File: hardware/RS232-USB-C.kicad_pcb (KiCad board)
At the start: 2 copper layers, 85.6 x 30.5 mm, 68 parts, among them J1 USB_C_Receptacle_USB2.0_16P, J10 NC, J11 UART, J12 NC, J13 NC, J2 DE9_Receptacle, J3* NC, J4 RXTX, J5 RTSCTS, J6 DTRDSR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

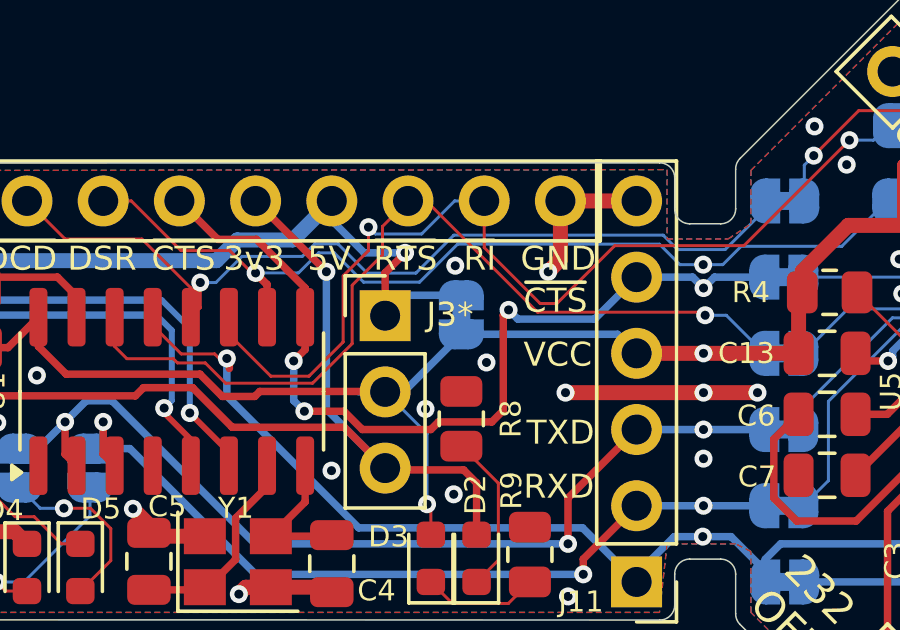
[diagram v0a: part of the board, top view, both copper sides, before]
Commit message: Tidy schematic
- Replaced criss-crossed wires with labels between IC/connectors
- Removed jumper 'values' where wasn't really needed
- repositioned references/values where hard to read
- gave components room to 'breathe'
- changed to regular (compared to small) components in most places to avoid cramping
- moved components around to be close to their logical section
- updated some symbols to be more standard/correct
- replaced 'NC' components to regularly labelled ones marked as DNP
- fixed sch->pcb linking on J3
- organized schematic into logical blocks
- uncommited the lockfile
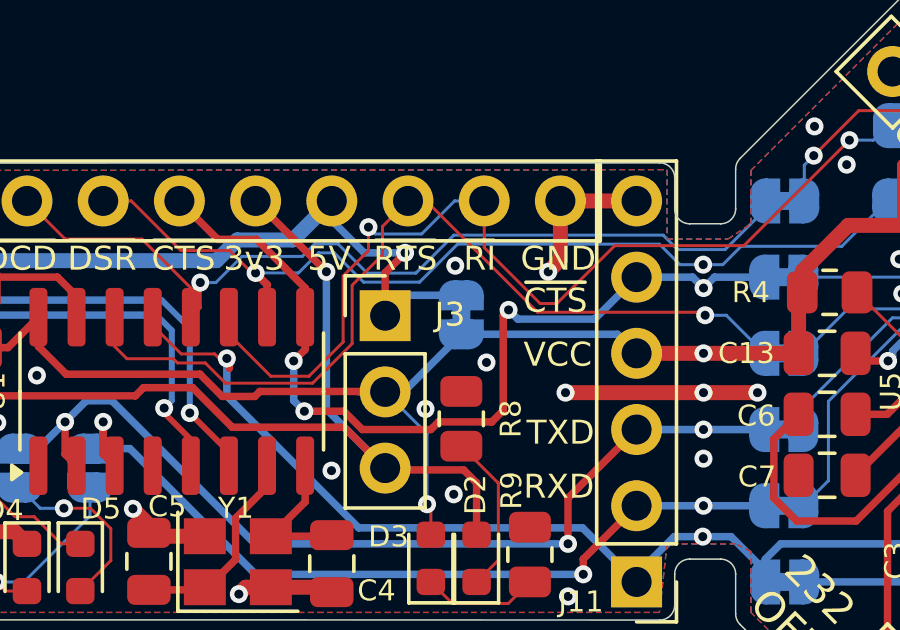
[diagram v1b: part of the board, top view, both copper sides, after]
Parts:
- J1: value USB_C_Receptacle_USB2.0_16P -> HOST
- J10: value NC -> SHUTDOWN
- J11: value UART -> FTDI_HEADER
- J12: value NC -> UART BUS
- J13: value NC -> EXT_PWR
- J3: renamed from J3*; value NC -> PWR_SEL
- J8: value NC -> RS232
- J9: value NC -> USB
- R3: value NC -> 5k1
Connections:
- net /VBUS renamed VBUS
- net /~{232STS} renamed Net-(U5-~{STATUS})
- net 232CTS renamed /232CTS
- net 232DCD renamed /232DCD
- net 232DSR renamed /232DSR
- net 232DTR renamed /232DTR
- net 232RI renamed /232RI
- net 232RTS renamed /232RTS
- net 232RxD renamed /232RxD
- net 232TxD renamed /232TxD
- net Net-(J1-CC1) renamed /CC1
- net Net-(J1-CC2) renamed /CC2
- net Net-(J1-SBU1) renamed /SBU1
- net Net-(J1-SBU2) renamed /SBU2
- net Net-(J1-SHIELD) renamed SHIELD
- net Net-(J4-Pin_2) renamed /DE9_P2
- net Net-(J4-Pin_3) renamed /DE9_P3
- net Net-(J5-Pin_2) renamed /DE9_P7
- net Net-(J5-Pin_3) renamed /DE9_P8
- net Net-(J6-Pin_2) renamed /DE9_P4
- net Net-(J6-Pin_3) renamed /DE9_P6
- net Net-(J7-Pin_2) renamed /DE9_P1
- net Net-(J9-Pin_5) renamed /D-B
- net Net-(J9-Pin_6) renamed /D+A
- net Net-(J9-Pin_7) renamed /D-A
- net Net-(J9-Pin_8) renamed /D+B
- net Net-(U1-XI) renamed /XI
- net Net-(U1-XO) renamed /XO
- J10 pad 1: GND -> /~{232SHD}
- J10 pad 2: /~{232SHD} -> GND
- J2 pad 0: (no net) -> GND
- J8 pad 10: (no net) -> unconnected-(J8-Pin_10-Pad10)
- J8 pad 5: GND -> /DE9_P5
- R5 pad 1: /3VEN -> Net-(U3-EN)
- U3 pad 3: /3VEN -> Net-(U3-EN)
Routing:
- net /DE9_P5: track 0.00 -> 12.0 mm
- net GND: track 110.7 -> 98.7 mm

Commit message: Rev 1
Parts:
- added C9: 100nF, Capacitor_SMD:C_0805_2012Metric, F.Cu at (137.4, 90.4)
- added JP24: 3v3 opt., Jumper:SolderJumper-2_P1.3mm_Open_RoundedPad1.0x1.5mm, B.Cu at (143.4, 88.9)
- moved J10 2.52 mm to (174.8, 96.0), turned to 45 degrees
- moved JP17 1.12 mm to (127.8, 92.7)
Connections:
- J8 pad 5: /DE9_P5 -> GND
- J9 pad 12: SHIELD -> +3V3
- R5 pad 1: Net-(U3-EN) -> /3VEN
- U1 pad 4: unconnected-(U1-V3-Pad4) -> Net-(JP24-A)
- U3 pad 3: Net-(U3-EN) -> /3VEN
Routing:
- net Net-(JP24-A): track 0.00 -> 17.1 mm, vias 0 -> 2
- net GND: track 98.7 -> 114.1 mm, vias 39 -> 47
- net +3V3: track 39.8 -> 54.9 mm, vias 1 -> 3
- net /DE9_P5: track 12.0 -> 0.00 mm
- net SHIELD: track 30.3 -> 22.4 mm
- net Net-(D5-K): track 7.35 -> 4.78 mm, vias 1 -> 0
- net VCC: track 55.5 -> 58.0 mm, vias 3 -> 4
- net /DE9_P8: track 27.0 -> 27.7 mm
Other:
- board text added: "*Cut JP1 if using J3 to switch VCC"
- board text added: "Rev.1"
- board text removed: "*Cut JP1 before using J3 to switch VCC"
